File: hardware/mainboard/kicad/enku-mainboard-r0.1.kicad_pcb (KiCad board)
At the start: 4 copper layers, 54 x 94 mm, 122 parts, among them J1 1S LiPo + NTC, J2 Hirose DM3AT-SF-PEJM5, J3 FH34SRJ-24S-0.5SH(50), J5 GCT USB4105-GF-A-120, J6 4-pin pogo dock, J7 Tag-Connect TC2030-IDC-NL, Q1 IRLML6346TRPBF, SW1 HARD POWER, SW2 BOOT / RECOVERY, SW3 BTN_L1, SW4 BTN_L2, SW5 BTN_R1, SW6 BTN_R2, U1 ESP32-S3-WROOM-1-N16R8, U2 TPS2121, U3 BQ25185DLHR, U4 TPS63802DLAR, U5 BMI270, U6 DRV5032FBDBZR, U8 USBLC6-2SC6

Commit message: pcb: reconnect MUX_PR1 sense endpoint
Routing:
- net MUX_PR1: track 59.0 -> 59.8 mm
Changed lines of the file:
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@@
   (via (at 71.20 79.60) (size 0.60) (drill 0.30) (layers "F.Cu" "In2.Cu") (net 82))
   (segment (start 71.20 79.60) (end 71.20 81.40) (width 0.18) (layer "F.Cu") (net 82))
+  (segment (start 71.20 80.50) (end 70.40 80.50) (width 0.18) (layer "F.Cu") (net 82))
   (segment (start 71.20 81.40) (end 63.20 82.00) (width 0.18) (layer "F.Cu") (net 82))
   (segment (start 43.75 89.85) (end 44.50 89.85) (width 0.18) (layer "F.Cu") (net 87))

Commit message: pcb: move local MUX_PR1 escape left of USB spine
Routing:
- net MUX_PR1: track 59.8 -> 60.8 mm
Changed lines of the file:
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@@
   (via (at 70.00 83.20) (size 0.60) (drill 0.30) (layers "F.Cu" "In2.Cu") (net 84))
   (segment (start 70.00 83.20) (end 71.40 82.00) (width 0.18) (layer "F.Cu") (net 84))
-  (segment (start 44.25 92.15) (end 45.00 93.00) (width 0.18) (layer "F.Cu") (net 82))
-  (segment (start 45.00 93.00) (end 45.00 94.50) (width 0.18) (layer "F.Cu") (net 82))
-  (via (at 45.00 94.50) (size 0.60) (drill 0.30) (layers "F.Cu" "In2.Cu") (net 82))
-  (segment (start 45.00 94.50) (end 52.50 95.00) (width 0.18) (layer "In2.Cu") (net 82))
+  (segment (start 44.25 92.15) (end 43.80 93.00) (width 0.18) (layer "F.Cu") (net 82))
+  (segment (start 43.80 93.00) (end 43.80 94.50) (width 0.18) (layer "F.Cu") (net 82))
+  (via (at 43.80 94.50) (size 0.60) (drill 0.30) (layers "F.Cu" "In2.Cu") (net 82))
+  (segment (start 43.80 94.50) (end 52.50 95.00) (width 0.18) (layer "In2.Cu") (net 82))
   (segment (start 52.50 95.00) (end 52.50 76.80) (width 0.18) (layer "In2.Cu") (net 82))
   (segment (start 52.50 76.80) (end 70.40 76.80) (width 0.18) (layer "In2.Cu") (net 82))

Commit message: pcb: restore confirmed 822-DRC baseline
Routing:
- net VBUS_USB: track 94.1 -> 80.3 mm
- net MUX_PR1: track 60.8 -> 57.3 mm
- net VBUS_DOCK: vias 3 -> 2
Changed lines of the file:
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@@
   (segment (start 45.50 96.50) (end 41.20 96.50) (width 0.50) (layer "B.Cu") (net 79))
   (segment (start 41.20 96.50) (end 41.20 91.35) (width 0.50) (layer "B.Cu") (net 79))
-  (via (at 41.20 91.35) (size 0.80) (drill 0.40) (layers "F.Cu" "In2.Cu") (net 79))
+  (via (at 41.20 91.35) (size 0.80) (drill 0.40) (layers "F.Cu" "B.Cu") (net 79))
   (segment (start 41.20 91.35) (end 42.825 91.35) (width 0.20) (layer "F.Cu") (net 79))
   (via (at 44.60 105.30) (size 0.80) (drill 0.40) (layers "F.Cu" "B.Cu") (net 3))
@@
   (via (at 34.30 92.50) (size 0.80) (drill 0.40) (layers "F.Cu" "B.Cu") (net 3))
   (segment (start 34.30 92.50) (end 35.50 92.50) (width 0.45) (layer "F.Cu") (net 3))
-  (segment (start 34.30 92.50) (end 34.30 95.30) (width 0.50) (layer "B.Cu") (net 3))
-  (segment (start 34.30 95.30) (end 45.30 95.30) (width 0.50) (layer "B.Cu") (net 3))
   (segment (start 48.75 106.645) (end 48.75 105.55) (width 0.18) (layer "F.Cu") (net 5))
   (segment (start 48.75 105.55) (end 48.20 105.00) (width 0.18) (layer "F.Cu") (net 5))
@@
   (via (at 70.00 83.20) (size 0.60) (drill 0.30) (layers "F.Cu" "In2.Cu") (net 84))
   (segment (start 70.00 83.20) (end 71.40 82.00) (width 0.18) (layer "F.Cu") (net 84))
-  (segment (start 44.25 92.15) (end 43.80 93.00) (width 0.18) (layer "F.Cu") (net 82))
-  (segment (start 43.80 93.00) (end 43.80 94.50) (width 0.18) (layer "F.Cu") (net 82))
-  (via (at 43.80 94.50) (size 0.60) (drill 0.30) (layers "F.Cu" "In2.Cu") (net 82))
-  (segment (start 43.80 94.50) (end 52.50 95.00) (width 0.18) (layer "In2.Cu") (net 82))
+  (segment (start 44.25 92.15) (end 45.00 93.00) (width 0.18) (layer "F.Cu") (net 82))
+  (segment (start 45.00 93.00) (end 45.00 94.50) (width 0.18) (layer "F.Cu") (net 82))
+  (via (at 45.00 94.50) (size 0.60) (drill 0.30) (layers "F.Cu" "In2.Cu") (net 82))
+  (segment (start 45.00 94.50) (end 52.50 95.00) (width 0.18) (layer "In2.Cu") (net 82))
   (segment (start 52.50 95.00) (end 52.50 76.80) (width 0.18) (layer "In2.Cu") (net 82))
   (segment (start 52.50 76.80) (end 70.40 76.80) (width 0.18) (layer "In2.Cu") (net 82))
-  (segment (start 70.40 76.80) (end 71.20 79.60) (width 0.18) (layer "In2.Cu") (net 82))
-  (via (at 71.20 79.60) (size 0.60) (drill 0.30) (layers "F.Cu" "In2.Cu") (net 82))
-  (segment (start 71.20 79.60) (end 71.20 81.40) (width 0.18) (layer "F.Cu") (net 82))
-  (segment (start 71.20 80.50) (end 70.40 80.50) (width 0.18) (layer "F.Cu") (net 82))
-  (segment (start 71.20 81.40) (end 63.20 82.00) (width 0.18) (layer "F.Cu") (net 82))
+  (segment (start 70.40 76.80) (end 70.40 80.50) (width 0.18) (layer "In2.Cu") (net 82))
+  (via (at 70.40 80.50) (size 0.60) (drill 0.30) (layers "F.Cu" "In2.Cu") (net 82))
+  (segment (start 70.40 80.50) (end 63.20 82.00) (width 0.18) (layer "F.Cu") (net 82))
   (segment (start 43.75 89.85) (end 44.50 89.85) (width 0.18) (layer "F.Cu") (net 87))
   (via (at 44.50 89.85) (size 0.60) (drill 0.30) (layers "F.Cu" "In2.Cu") (net 87))
@@
   (segment (start 68.800 80.500) (end 68.000 80.500) (width 0.35) (layer "F.Cu") (net 3))
   (via (at 68.000 80.500) (size 0.70) (drill 0.35) (layers "F.Cu" "B.Cu") (net 3))
-  (segment (start 68.000 80.500) (end 68.000 81.200) (width 0.35) (layer "B.Cu") (net 3))
-  (segment (start 68.000 81.200) (end 45.500 81.200) (width 0.35) (layer "B.Cu") (net 3))
-  (segment (start 45.500 81.200) (end 45.500 91.500) (width 0.35) (layer "B.Cu") (net 3))
+  (segment (start 68.000 80.500) (end 45.500 80.500) (width 0.35) (layer "B.Cu") (net 3))
+  (segment (start 45.500 80.500) (end 45.500 91.500) (width 0.35) (layer "B.Cu") (net 3))
   (segment (start 45.500 91.500) (end 45.300 91.500) (width 0.35) (layer "B.Cu") (net 3))
   (segment (start 66.000 82.000) (end 66.000 83.000) (width 0.35) (layer "F.Cu") (net 79))
   (via (at 66.000 83.000) (size 0.70) (drill 0.35) (layers "F.Cu" "B.Cu") (net 79))
   (segment (start 66.000 83.000) (end 49.000 83.000) (width 0.35) (layer "B.Cu") (net 79))
-  (segment (start 49.000 83.000) (end 49.000 89.000) (width 0.35) (layer "B.Cu") (net 79))
-  (via (at 49.000 89.000) (size 0.70) (drill 0.35) (layers "B.Cu" "In2.Cu") (net 79))
-  (segment (start 49.000 89.000) (end 41.200 89.000) (width 0.35) (layer "In2.Cu") (net 79))
-  (segment (start 41.200 89.000) (end 41.200 91.350) (width 0.35) (layer "In2.Cu") (net 79))
+  (segment (start 49.000 83.000) (end 49.000 91.350) (width 0.35) (layer "B.Cu") (net 79))
+  (segment (start 49.000 91.350) (end 41.200 91.350) (width 0.35) (layer "B.Cu") (net 79))
   (segment (start 28.000 65.000) (end 29.000 65.000) (width 0.18) (layer "F.Cu") (net 23))
   (segment (start 29.000 65.000) (end 55.000 65.000) (width 0.18) (layer "F.Cu") (net 23))

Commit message: pcb: rebuild USB D+/D- as paired bottom-layer corridor
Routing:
- net USB_DP: track 127.7 -> 81.2 mm
- net USB_DM: track 108.8 -> 80.9 mm
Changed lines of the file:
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@@
   (via (at 41.71 55.20) (size 0.60) (drill 0.30) (layers "F.Cu" "In1.Cu") (net 56))
   (segment (start 42.98 53.75) (end 42.98 55.20) (width 0.18) (layer "F.Cu") (net 57))
-  (via (at 42.98 55.20) (size 0.60) (drill 0.30) (layers "F.Cu" "In1.Cu") (net 57))
-  (via (at 63.80 100.00) (size 0.60) (drill 0.30) (layers "F.Cu" "In1.Cu") (net 57))
+  (via (at 42.98 55.20) (size 0.60) (drill 0.30) (layers "F.Cu" "B.Cu") (net 57))
+  (segment (start 42.98 55.20) (end 42.98 56.40) (width 0.18) (layer "B.Cu") (net 57))
+  (segment (start 42.98 56.40) (end 70.20 56.40) (width 0.18) (layer "B.Cu") (net 57))
+  (segment (start 70.20 56.40) (end 70.20 99.20) (width 0.18) (layer "B.Cu") (net 57))
+  (segment (start 70.20 99.20) (end 63.80 99.20) (width 0.18) (layer "B.Cu") (net 57))
+  (via (at 63.80 99.20) (size 0.60) (drill 0.30) (layers "F.Cu" "B.Cu") (net 57))
+  (segment (start 63.80 99.20) (end 63.80 100.50) (width 0.18) (layer "F.Cu") (net 57))
+  (via (at 44.25 55.20) (size 0.60) (drill 0.30) (layers "F.Cu" "B.Cu") (net 58))
+  (segment (start 44.25 55.20) (end 44.25 57.10) (width 0.18) (layer "B.Cu") (net 58))
+  (segment (start 44.25 57.10) (end 69.40 57.10) (width 0.18) (layer "B.Cu") (net 58))
+  (segment (start 69.40 57.10) (end 69.40 98.40) (width 0.18) (layer "B.Cu") (net 58))
+  (segment (start 69.40 98.40) (end 60.80 98.40) (width 0.18) (layer "B.Cu") (net 58))
+  (via (at 60.80 98.40) (size 0.60) (drill 0.30) (layers "F.Cu" "B.Cu") (net 58))
+  (segment (start 60.80 98.40) (end 60.80 100.50) (width 0.18) (layer "F.Cu") (net 58))
   (segment (start 63.80 100.00) (end 63.80 100.50) (width 0.18) (layer "F.Cu") (net 57))
   (segment (start 44.25 53.75) (end 44.25 55.20) (width 0.18) (layer "F.Cu") (net 58))
-  (via (at 44.25 55.20) (size 0.60) (drill 0.30) (layers "F.Cu" "In2.Cu") (net 58))
-  (segment (start 44.25 55.20) (end 20.60 57.20) (width 0.18) (layer "In2.Cu") (net 58))
-  (segment (start 20.60 57.20) (end 20.60 110.00) (width 0.18) (layer "In2.Cu") (net 58))
-  (segment (start 20.60 110.00) (end 60.80 110.00) (width 0.18) (layer "In2.Cu") (net 58))
-  (segment (start 60.80 110.00) (end 60.80 101.20) (width 0.18) (layer "In2.Cu") (net 58))
-  (via (at 60.80 101.20) (size 0.60) (drill 0.30) (layers "F.Cu" "In2.Cu") (net 58))
   (segment (start 60.80 101.20) (end 60.80 100.50) (width 0.18) (layer "F.Cu") (net 58))
   (segment (start 45.50 49.445) (end 47.00 49.445) (width 0.18) (layer "F.Cu") (net 59))
@@
   (via (at 23.200 85.175) (size 0.60) (drill 0.30) (layers "F.Cu" "In1.Cu") (net 56))
   (segment (start 23.200 85.175) (end 24.000 85.175) (width 0.18) (layer "F.Cu") (net 56))
-  (segment (start 42.98 55.20) (end 21.40 57.20) (width 0.18) (layer "In1.Cu") (net 57))
-  (segment (start 21.40 57.20) (end 21.40 100.00) (width 0.18) (layer "In1.Cu") (net 57))
-  (segment (start 21.40 100.00) (end 63.80 100.00) (width 0.18) (layer "In1.Cu") (net 57))
   (segment (start 32.820 37.200) (end 32.820 79.000) (width 0.18) (layer "B.Cu") (net 70))
   (segment (start 32.820 79.000) (end 28.500 79.000) (width 0.18) (layer "B.Cu") (net 70))

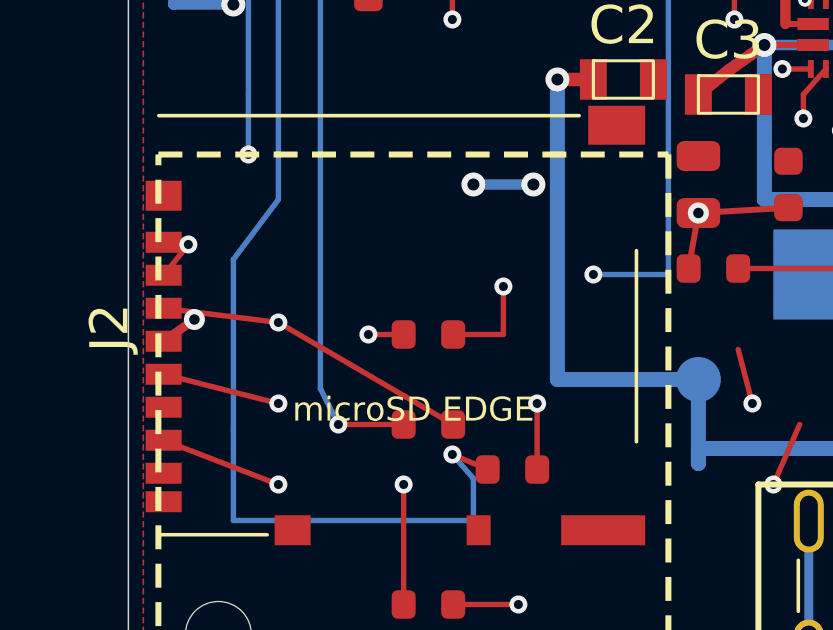
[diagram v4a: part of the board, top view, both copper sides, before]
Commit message: pcb: lift SD_CS trunk out of USB and battery corridor
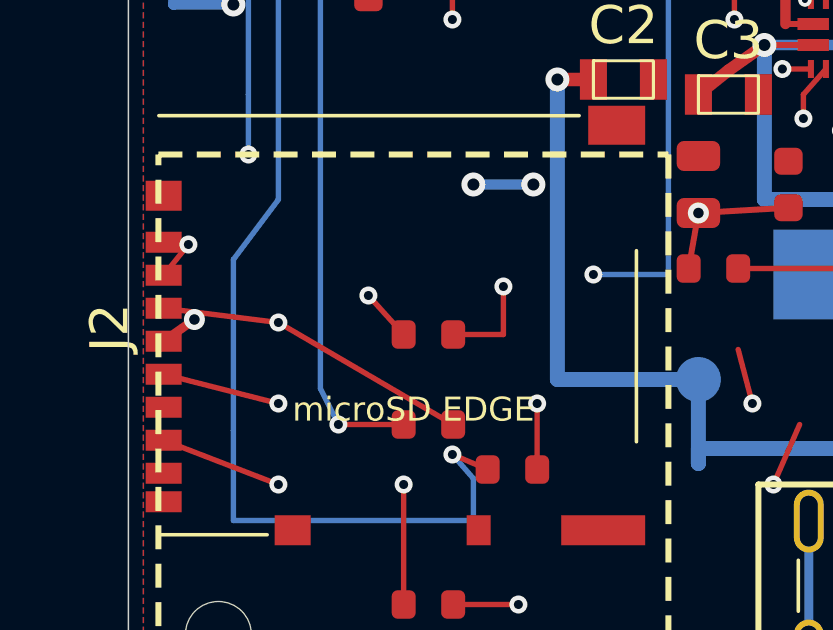
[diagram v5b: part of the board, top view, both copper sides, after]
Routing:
- net SD_CS: track 127.0 -> 128.9 mm
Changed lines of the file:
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@@
   (segment (start 73.300 101.500) (end 72.000 101.500) (width 0.18) (layer "B.Cu") (net 60))
   (via (at 72.000 101.500) (size 0.60) (drill 0.30) (layers "B.Cu" "In1.Cu") (net 60))
-  (segment (start 72.000 101.500) (end 28.000 101.500) (width 0.18) (layer "In1.Cu") (net 60))
-  (segment (start 28.000 101.500) (end 28.000 101.000) (width 0.18) (layer "In1.Cu") (net 60))
-  (via (at 28.000 101.000) (size 0.60) (drill 0.30) (layers "F.Cu" "In1.Cu") (net 60))
-  (segment (start 28.000 101.000) (end 29.175 101.000) (width 0.18) (layer "F.Cu") (net 60))
+  (segment (start 72.000 101.500) (end 72.000 99.700) (width 0.18) (layer "In1.Cu") (net 60))
+  (segment (start 72.000 99.700) (end 28.000 99.700) (width 0.18) (layer "In1.Cu") (net 60))
+  (via (at 28.000 99.700) (size 0.60) (drill 0.30) (layers "F.Cu" "In1.Cu") (net 60))
+  (segment (start 28.000 99.700) (end 29.175 101.000) (width 0.18) (layer "F.Cu") (net 60))
   (segment (start 41.71 53.75) (end 41.71 55.20) (width 0.18) (layer "F.Cu") (net 56))
   (via (at 41.71 55.20) (size 0.60) (drill 0.30) (layers "F.Cu" "In1.Cu") (net 56))

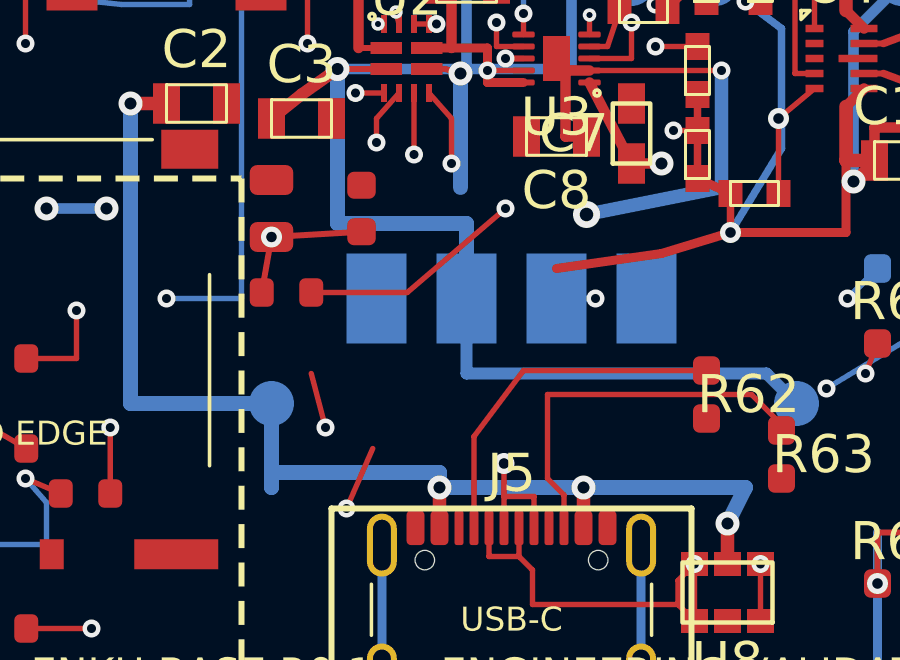
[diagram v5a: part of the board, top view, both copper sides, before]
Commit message: pcb: reconnect split VBUS_USB power tree
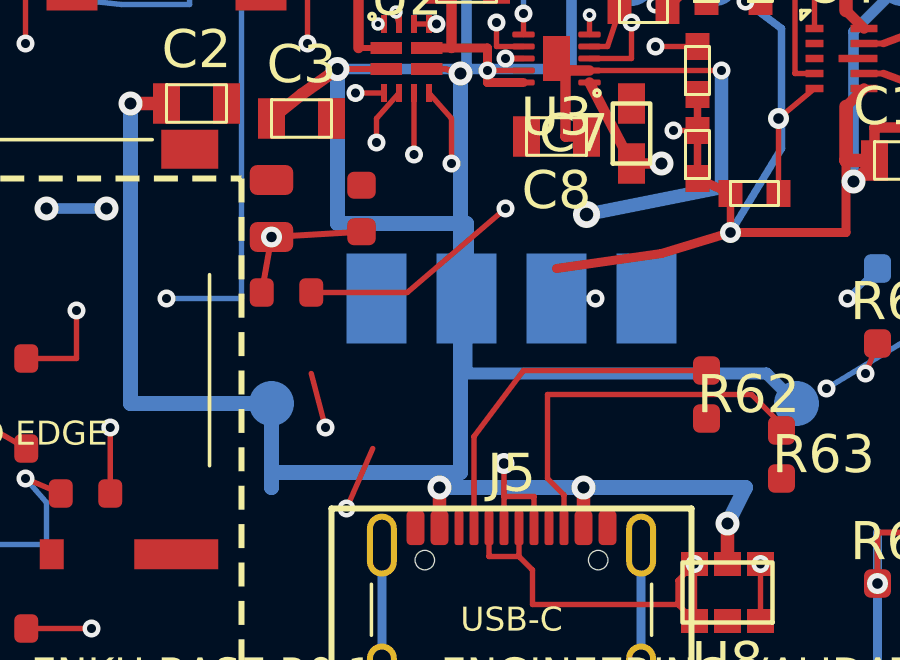
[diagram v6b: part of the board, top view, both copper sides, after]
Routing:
- net VBUS_USB: track 80.3 -> 90.5 mm
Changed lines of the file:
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@@
   (segment (start 49.40 105.30) (end 54.80 105.30) (width 0.50) (layer "B.Cu") (net 3))
   (segment (start 45.30 95.30) (end 45.30 91.50) (width 0.50) (layer "B.Cu") (net 3))
+  (segment (start 45.30 95.30) (end 45.30 104.80) (width 0.50) (layer "B.Cu") (net 3))
+  (segment (start 45.30 104.80) (end 44.60 104.80) (width 0.50) (layer "B.Cu") (net 3))
   (via (at 45.30 91.50) (size 0.80) (drill 0.40) (layers "F.Cu" "B.Cu") (net 3))
   (segment (start 45.30 91.50) (end 44.80 91.35) (width 0.20) (layer "F.Cu") (net 3))

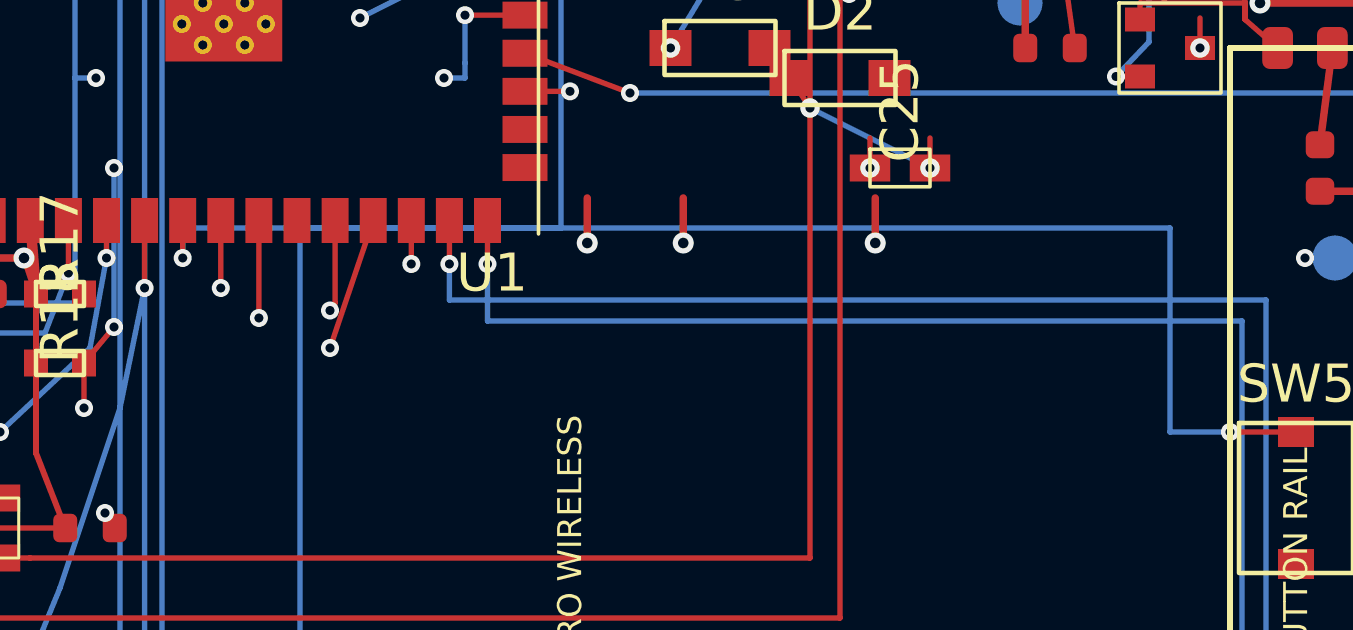
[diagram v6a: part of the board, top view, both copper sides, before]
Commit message: pcb: lift BTN_R1 trunk clear of SPI MISO and 3V3 vias
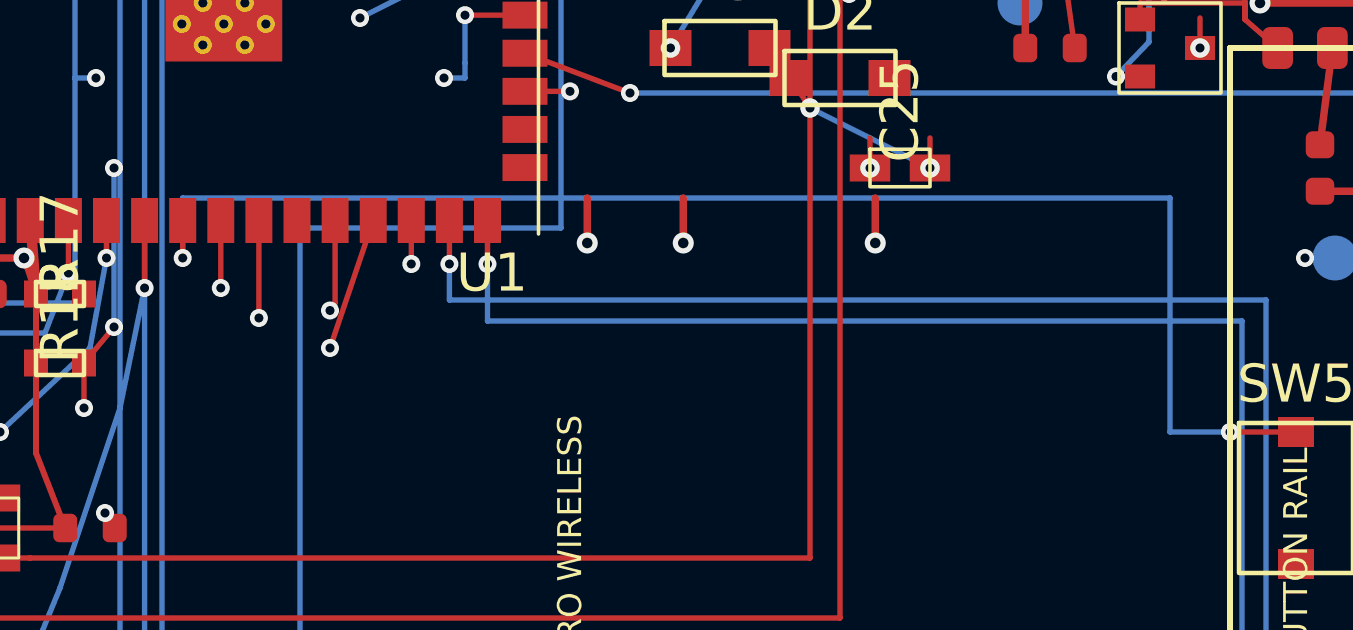
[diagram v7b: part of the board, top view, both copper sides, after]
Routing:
- net BTN_R1: track 46.2 -> 48.2 mm
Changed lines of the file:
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@@
   (segment (start 32.000 70.000) (end 32.000 44.000) (width 0.18) (layer "B.Cu") (net 18))
   (segment (start 32.000 44.000) (end 42.500 44.000) (width 0.18) (layer "B.Cu") (net 18))
-  (segment (start 34.09 55.00) (end 34.09 54.00) (width 0.18) (layer "B.Cu") (net 50))
-  (segment (start 34.09 54.00) (end 67.00 54.00) (width 0.18) (layer "B.Cu") (net 50))
-  (segment (start 67.00 54.00) (end 67.00 60.80) (width 0.18) (layer "B.Cu") (net 50))
+  (segment (start 34.09 55.00) (end 34.09 53.00) (width 0.18) (layer "B.Cu") (net 50))
+  (segment (start 34.09 53.00) (end 67.00 53.00) (width 0.18) (layer "B.Cu") (net 50))
+  (segment (start 67.00 53.00) (end 67.00 60.80) (width 0.18) (layer "B.Cu") (net 50))
   (segment (start 67.00 60.80) (end 69.00 60.80) (width 0.18) (layer "B.Cu") (net 50))
 )

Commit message: pcb: close remaining 3V3 decoupling split
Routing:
- net 3V3_SYS: track 288.3 -> 296.9 mm
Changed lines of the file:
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@@
   (segment (start 23.000 77.775) (end 23.000 80.775) (width 0.35) (layer "In2.Cu") (net 2))
   (segment (start 23.000 80.775) (end 23.000 83.825) (width 0.35) (layer "In2.Cu") (net 2))
+  (segment (start 23.000 80.775) (end 31.500 82.000) (width 0.25) (layer "In2.Cu") (net 2))
   (segment (start 23.000 83.825) (end 23.000 86.825) (width 0.35) (layer "In2.Cu") (net 2))
   (via (at 23.000 80.775) (size 0.70) (drill 0.35) (layers "F.Cu" "In2.Cu") (net 2))
